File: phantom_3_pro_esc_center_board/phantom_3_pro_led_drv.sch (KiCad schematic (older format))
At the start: 14 parts

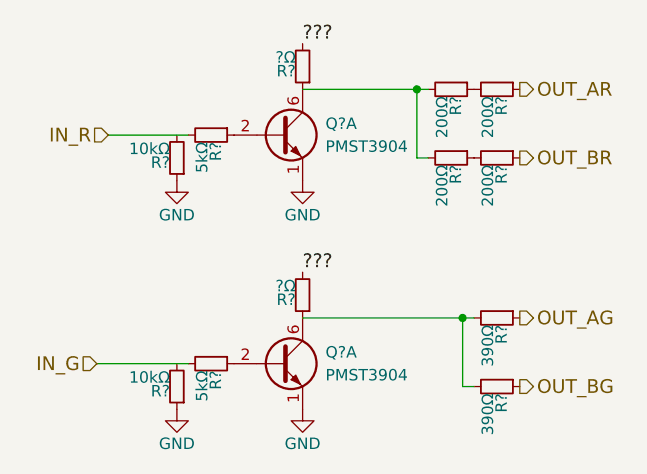
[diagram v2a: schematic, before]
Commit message: ESC Center: Formed a link between schematic and PCB.
Modified PCB to link some components to schematic.

Also created edge pad connectors to FC board.
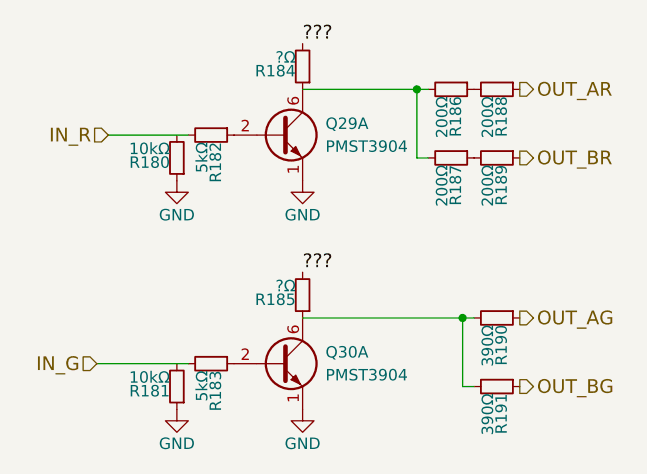
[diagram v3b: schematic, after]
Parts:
- gave numbers to parts that had none: 14
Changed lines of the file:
@@
 EESchema Schematic File Version 2
+LIBS:conn-v2
 LIBS:power
 LIBS:device
@@
 $EndDescr
 $Comp
-L R_Small R?
+L R_Small R174
 U 1 1 5977AACE
 P 2800 900
-F 0 "R?" H 2830 920 50  0000 L CNN
+AR Path="/5977925B/5977AACE" Ref="R174"  Part="1"
+AR Path="/5978542D/5977AACE" Ref="R186"  Part="1"
+F 0 "R186" H 2830 920 50  0000 L CNN
 F 1 "200Ω" H 2830 860 50  0000 L CNN
 F 2 "" H 2800 900 50  0001 C CNN
@@
 $EndComp
 $Comp
-L R_Small R?
+L R_Small R176
 U 1 1 5977AAD5
 P 3000 900
-F 0 "R?" H 3030 920 50  0000 L CNN
+AR Path="/5977925B/5977AAD5" Ref="R176"  Part="1"
+AR Path="/5978542D/5977AAD5" Ref="R188"  Part="1"
+F 0 "R188" H 3030 920 50  0000 L CNN
 F 1 "200Ω" H 3030 860 50  0000 L CNN
 F 2 "" H 3000 900 50  0001 C CNN
@@
 $EndComp
 $Comp
-L R_Small R?
+L R_Small R175
 U 1 1 5977AADC
 P 2800 1200
-F 0 "R?" H 2830 1220 50  0000 L CNN
+AR Path="/5977925B/5977AADC" Ref="R175"  Part="1"
+AR Path="/5978542D/5977AADC" Ref="R187"  Part="1"
+F 0 "R187" H 2830 1220 50  0000 L CNN
 F 1 "200Ω" H 2830 1160 50  0000 L CNN
 F 2 "" H 2800 1200 50  0001 C CNN
@@
 $EndComp
 $Comp
-L R_Small R?
+L R_Small R177
 U 1 1 5977AAE3
 P 3000 1200
-F 0 "R?" H 3030 1220 50  0000 L CNN
+AR Path="/5977925B/5977AAE3" Ref="R177"  Part="1"
+AR Path="/5978542D/5977AAE3" Ref="R189"  Part="1"
+F 0 "R189" H 3030 1220 50  0000 L CNN
 F 1 "200Ω" H 3030 1160 50  0000 L CNN
 F 2 "" H 3000 1200 50  0001 C CNN
@@
 $EndComp
 $Comp
-L R_Small R?
+L R_Small R178
 U 1 1 5977AB06
 P 3000 1900
-F 0 "R?" H 3030 1920 50  0000 L CNN
+AR Path="/5977925B/5977AB06" Ref="R178"  Part="1"
+AR Path="/5978542D/5977AB06" Ref="R190"  Part="1"
+F 0 "R190" H 3030 1920 50  0000 L CNN
 F 1 "390Ω" H 3030 1860 50  0000 L CNN
 F 2 "" H 3000 1900 50  0001 C CNN
@@
 $EndComp
 $Comp
-L R_Small R?
+L R_Small R179
 U 1 1 5977AB0D
 P 3000 2200
-F 0 "R?" H 3030 2220 50  0000 L CNN
+AR Path="/5977925B/5977AB0D" Ref="R179"  Part="1"
+AR Path="/5978542D/5977AB0D" Ref="R191"  Part="1"
+F 0 "R191" H 3030 2220 50  0000 L CNN
 F 1 "390Ω" H 3030 2160 50  0000 L CNN
 F 2 "" H 3000 2200 50  0001 C CNN
@@
 $EndComp
 $Comp
-L PMBT2222AYS Q?
+L PMBT2222AYS Q27
 U 1 1 5977AB14
 P 2050 1100
-F 0 "Q?" H 2250 1150 50  0000 L CNN
+AR Path="/5977925B/5977AB14" Ref="Q27"  Part="1"
+AR Path="/5978542D/5977AB14" Ref="Q29"  Part="1"
+F 0 "Q29" H 2250 1150 50  0000 L CNN
 F 1 "PMST3904" H 2250 1050 50  0000 L CNN
 F 2 "TO_SOT_Packages_SMD:SOT-363" H 2250 1200 50  0001 C CNN
@@
 $EndComp
 $Comp
-L PMBT2222AYS Q?
+L PMBT2222AYS Q28
 U 1 1 5977AB1B
 P 2050 2100
-F 0 "Q?" H 2250 2150 50  0000 L CNN
+AR Path="/5977925B/5977AB1B" Ref="Q28"  Part="1"
+AR Path="/5978542D/5977AB1B" Ref="Q30"  Part="1"
+F 0 "Q30" H 2250 2150 50  0000 L CNN
 F 1 "PMST3904" H 2250 2050 50  0000 L CNN
 F 2 "TO_SOT_Packages_SMD:SOT-363" H 2250 2200 50  0001 C CNN
@@
 Connection ~ 2850 1900
 $Comp
-L R_Small R?
+L R_Small R170
 U 1 1 5977AB2C
 P 1750 1100
-F 0 "R?" H 1780 1120 50  0000 L CNN
+AR Path="/5977925B/5977AB2C" Ref="R170"  Part="1"
+AR Path="/5978542D/5977AB2C" Ref="R182"  Part="1"
+F 0 "R182" H 1780 1120 50  0000 L CNN
 F 1 "5kΩ" H 1780 1060 50  0000 L CNN
 F 2 "" H 1750 1100 50  0001 C CNN
@@
 $EndComp
 $Comp
-L R_Small R?
+L R_Small R171
 U 1 1 5977AB33
 P 1750 2100
-F 0 "R?" H 1780 2120 50  0000 L CNN
+AR Path="/5977925B/5977AB33" Ref="R171"  Part="1"
+AR Path="/5978542D/5977AB33" Ref="R183"  Part="1"
+F 0 "R183" H 1780 2120 50  0000 L CNN
 F 1 "5kΩ" H 1780 2060 50  0000 L CNN
 F 2 "" H 1750 2100 50  0001 C CNN
@@
 	1650 2100 1250 2100
 $Comp
-L R_Small R?
+L R_Small R168
 U 1 1 5977AB3E
 P 1600 1200
-F 0 "R?" H 1630 1220 50  0000 L CNN
+AR Path="/5977925B/5977AB3E" Ref="R168"  Part="1"
+AR Path="/5978542D/5977AB3E" Ref="R180"  Part="1"
+F 0 "R180" H 1630 1220 50  0000 L CNN
 F 1 "10kΩ" H 1630 1160 50  0000 L CNN
 F 2 "" H 1600 1200 50  0001 C CNN
@@
 $EndComp
 $Comp
-L GND #PWR?
+L GND #PWR0215
 U 1 1 5977AB45
 P 1600 1300
-F 0 "#PWR?" H 1600 1050 50  0001 C CNN
+AR Path="/5977925B/5977AB45" Ref="#PWR0215"  Part="1"
+AR Path="/5978542D/5977AB45" Ref="#PWR0219"  Part="1"
+F 0 "#PWR0219" H 1600 1050 50  0001 C CNN
 F 1 "GND" H 1600 1150 50  0000 C CNN
 F 2 "" H 1600 1300 50  0001 C CNN
@@
 $EndComp
 $Comp
-L GND #PWR?
+L GND #PWR0216
 U 1 1 5977AB4B
 P 2150 1300
-F 0 "#PWR?" H 2150 1050 50  0001 C CNN
+AR Path="/5977925B/5977AB4B" Ref="#PWR0216"  Part="1"
+AR Path="/5978542D/5977AB4B" Ref="#PWR0220"  Part="1"
+F 0 "#PWR0220" H 2150 1050 50  0001 C CNN
 F 1 "GND" H 2150 1150 50  0000 C CNN
 F 2 "" H 2150 1300 50  0001 C CNN
@@
 $EndComp
 $Comp
-L R_Small R?
+L R_Small R169
 U 1 1 5977AB51
 P 1600 2200
-F 0 "R?" H 1630 2220 50  0000 L CNN
+AR Path="/5977925B/5977AB51" Ref="R169"  Part="1"
+AR Path="/5978542D/5977AB51" Ref="R181"  Part="1"
+F 0 "R181" H 1630 2220 50  0000 L CNN
 F 1 "10kΩ" H 1630 2160 50  0000 L CNN
 F 2 "" H 1600 2200 50  0001 C CNN
@@
 $EndComp
 $Comp
-L GND #PWR?
+L GND #PWR0217
 U 1 1 5977AB58
 P 1600 2300
-F 0 "#PWR?" H 1600 2050 50  0001 C CNN
+AR Path="/5977925B/5977AB58" Ref="#PWR0217"  Part="1"
+AR Path="/5978542D/5977AB58" Ref="#PWR0221"  Part="1"
+F 0 "#PWR0221" H 1600 2050 50  0001 C CNN
 F 1 "GND" H 1600 2150 50  0000 C CNN
 F 2 "" H 1600 2300 50  0001 C CNN
@@
 $EndComp
 $Comp
-L GND #PWR?
+L GND #PWR0218
 U 1 1 5977AB5E
 P 2150 2300
-F 0 "#PWR?" H 2150 2050 50  0001 C CNN
+AR Path="/5977925B/5977AB5E" Ref="#PWR0218"  Part="1"
+AR Path="/5978542D/5977AB5E" Ref="#PWR0222"  Part="1"
+F 0 "#PWR0222" H 2150 2050 50  0001 C CNN
 F 1 "GND" H 2150 2150 50  0000 C CNN
 F 2 "" H 2150 2300 50  0001 C CNN
@@
 $EndComp
 $Comp
-L R_Small R?
+L R_Small R172
 U 1 1 5977AB64
 P 2150 800
-F 0 "R?" H 2180 820 50  0000 L CNN
+AR Path="/5977925B/5977AB64" Ref="R172"  Part="1"
+AR Path="/5978542D/5977AB64" Ref="R184"  Part="1"
+F 0 "R184" H 2180 820 50  0000 L CNN
 F 1 "?Ω" H 2180 760 50  0000 L CNN
 F 2 "" H 2150 800 50  0001 C CNN
@@
 $EndComp
 $Comp
-L R_Small R?
+L R_Small R173
 U 1 1 5977AB6B
 P 2150 1800
-F 0 "R?" H 2180 1820 50  0000 L CNN
+AR Path="/5977925B/5977AB6B" Ref="R173"  Part="1"
+AR Path="/5978542D/5977AB6B" Ref="R185"  Part="1"
+F 0 "R185" H 2180 1820 50  0000 L CNN
 F 1 "?Ω" H 2180 1760 50  0000 L CNN
 F 2 "" H 2150 1800 50  0001 C CNN

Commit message: All: Preparing for KiCad version change.
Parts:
- Q27, Q28: symbol PMBT2222AYS -> Transistor_BJT:PMBT2222AYS
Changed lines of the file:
@@
 $EndComp
 $Comp
-L PMBT2222AYS Q27
+L Transistor_BJT:PMBT2222AYS Q27
 U 1 1 5977AB14
 P 2050 1100
@@
 $EndComp
 $Comp
-L PMBT2222AYS Q28
+L Transistor_BJT:PMBT2222AYS Q28
 U 1 1 5977AB1B
 P 2050 2100

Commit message: ESC Center: Upgraded to KiCAD 5.0.1.
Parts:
- R168, R169, R170, R171, R172, R173, R174, R175, R176, R177, R178, R179: symbol R_Small -> Device:R_Small
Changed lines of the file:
@@
-EESchema Schematic File Version 2
-LIBS:conn-v2
-LIBS:power
-LIBS:device
-LIBS:transistors
-LIBS:conn
-LIBS:linear
-LIBS:regul
-LIBS:74xx
-LIBS:cmos4000
-LIBS:adc-dac
-LIBS:memory
-LIBS:xilinx
-LIBS:microcontrollers
-LIBS:dsp
-LIBS:microchip
-LIBS:analog_switches
-LIBS:motorola
-LIBS:texas
-LIBS:intel
-LIBS:audio
-LIBS:interface
-LIBS:digital-audio
-LIBS:philips
-LIBS:display
-LIBS:cypress
-LIBS:siliconi
-LIBS:opto
-LIBS:atmel
-LIBS:contrib
-LIBS:valves
-LIBS:DRV8301_DCA_56_thin
-LIBS:DRV8301_DCA_56
-LIBS:motors
-LIBS:motor_drivers
-LIBS:texas-uc
-LIBS:regul-v2
+EESchema Schematic File Version 4
 LIBS:phantom_3_pro_esc_center_board-cache
-EELAYER 25 0
+EELAYER 26 0
 EELAYER END
 $Descr A4 11693 8268
@@
 $EndDescr
 $Comp
-L R_Small R174
+L Device:R_Small R174
 U 1 1 5977AACE
 P 2800 900
@@
 $EndComp
 $Comp
-L R_Small R176
+L Device:R_Small R176
 U 1 1 5977AAD5
 P 3000 900
@@
 $EndComp
 $Comp
-L R_Small R175
+L Device:R_Small R175
 U 1 1 5977AADC
 P 2800 1200
@@
 $EndComp
 $Comp
-L R_Small R177
+L Device:R_Small R177
 U 1 1 5977AAE3
 P 3000 1200
@@
 $EndComp
 $Comp
-L R_Small R178
+L Device:R_Small R178
 U 1 1 5977AB06
 P 3000 1900
@@
 $EndComp
 $Comp
-L R_Small R179
+L Device:R_Small R179
 U 1 1 5977AB0D
 P 3000 2200
@@
 Connection ~ 2850 1900
 $Comp
-L R_Small R170
+L Device:R_Small R170
 U 1 1 5977AB2C
 P 1750 1100
@@
 $EndComp
 $Comp
-L R_Small R171
+L Device:R_Small R171
 U 1 1 5977AB33
 P 1750 2100
@@
 	1650 2100 1250 2100
 $Comp
-L R_Small R168
+L Device:R_Small R168
 U 1 1 5977AB3E
 P 1600 1200
@@
 $EndComp
 $Comp
-L GND #PWR0215
+L power:GND #PWR0215
 U 1 1 5977AB45
 P 1600 1300
@@
 $EndComp
 $Comp
-L GND #PWR0216
+L power:GND #PWR0216
 U 1 1 5977AB4B
 P 2150 1300
@@
 $EndComp
 $Comp
-L R_Small R169
+L Device:R_Small R169
 U 1 1 5977AB51
 P 1600 2200
@@
 $EndComp
 $Comp
-L GND #PWR0217
+L power:GND #PWR0217
 U 1 1 5977AB58
 P 1600 2300
@@
 $EndComp
 $Comp
-L GND #PWR0218
+L power:GND #PWR0218
 U 1 1 5977AB5E
 P 2150 2300
@@
 $EndComp
 $Comp
-L R_Small R172
+L Device:R_Small R172
 U 1 1 5977AB64
 P 2150 800
@@
 $EndComp
 $Comp
-L R_Small R173
+L Device:R_Small R173
 U 1 1 5977AB6B
 P 2150 1800
